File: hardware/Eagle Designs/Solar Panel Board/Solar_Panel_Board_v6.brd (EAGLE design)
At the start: 82.4 x 96.7 mm, 37 parts, among them J1 MOLEX_503763-0291MOLEX_503763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, J2 MOLEX_503763-0491MOLEX_503763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, J3 MOLEX_503763-0291MOLEX_503763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, U1 TMP36GSZ

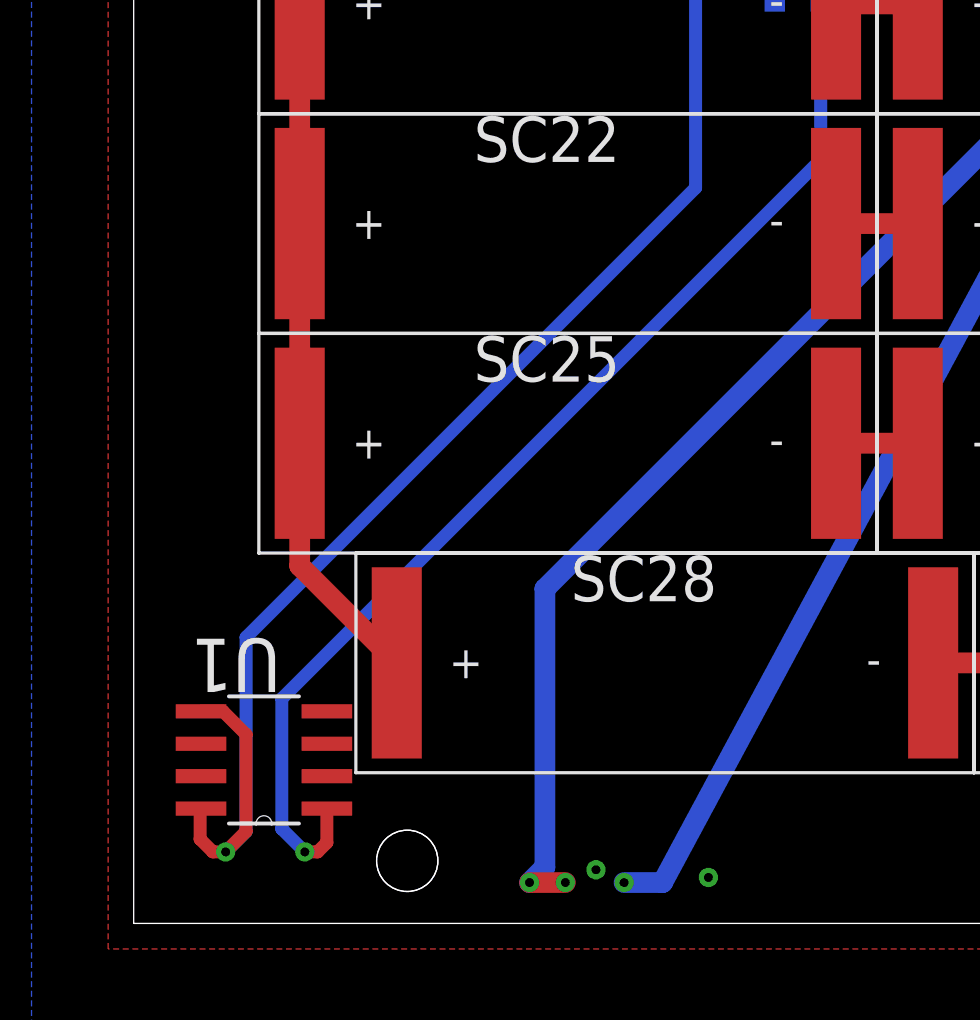
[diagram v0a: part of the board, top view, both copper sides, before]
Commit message: Updated OBC and Solar Panel boards
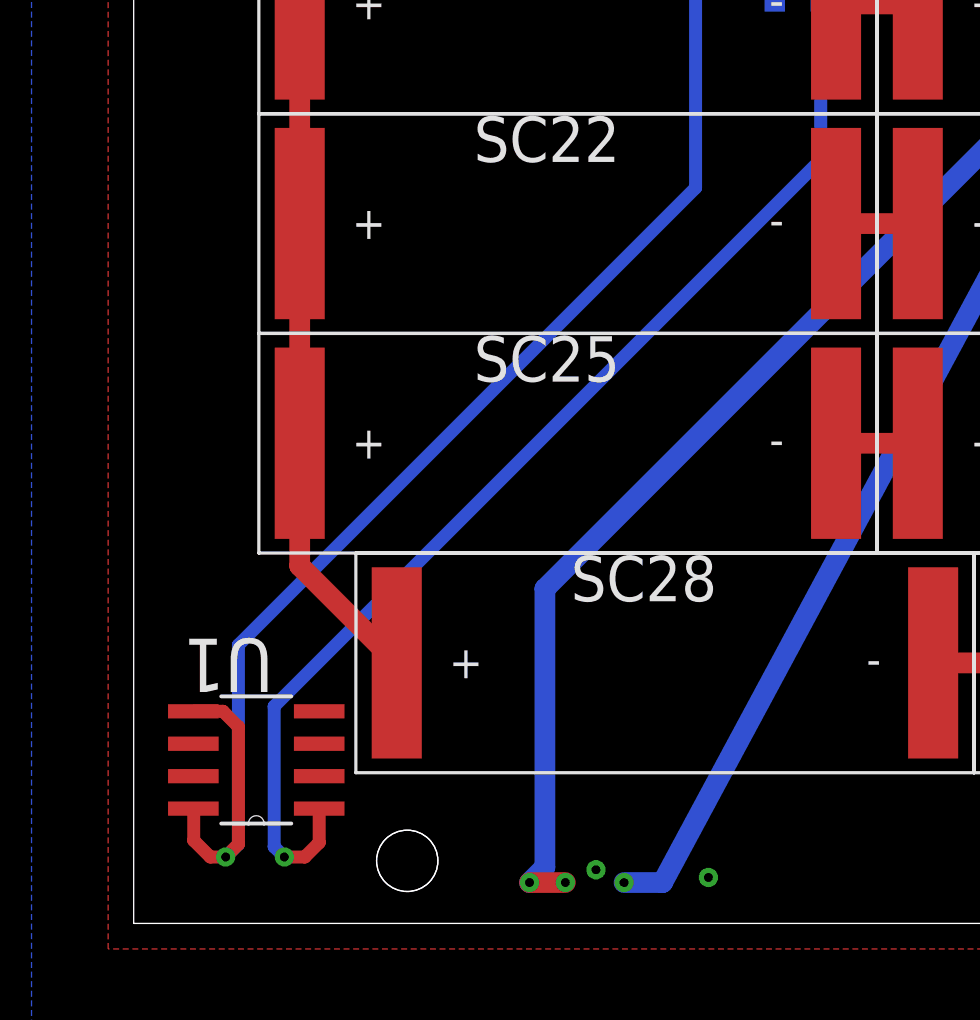
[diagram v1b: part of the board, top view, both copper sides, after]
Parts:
- moved U1 0.30 mm to (4.80, 6.40)
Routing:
- net VS+: track 84.2 -> 85.0 mm
- net N$12: track 45.0 -> 45.7 mm
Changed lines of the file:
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@@
 <attribute name="VOLTAGE_RATING" value="150V" x="43.6" y="70.8" size="1.778" layer="28" rot="MR0" display="off"/>
 </element>
-<element name="U1" library="TMP36GSZ" package="SOIC127P600X175-8N" value="TMP36GSZ" x="5.1" y="6.4" smashed="yes" rot="R180">
-<attribute name="NAME" x="5.760959375" y="11.146559375" size="2.08675" layer="25" ratio="10" rot="SR180"/>
-<attribute name="VALUE" x="8.55958125" y="12.12356875" size="2.08591875" layer="27" ratio="10" rot="SR180"/>
+<element name="U1" library="TMP36GSZ" package="SOIC127P600X175-8N" value="TMP36GSZ" x="4.8" y="6.4" smashed="yes" rot="R180">
+<attribute name="NAME" x="5.460959375" y="11.146559375" size="2.08675" layer="25" ratio="10" rot="SR180"/>
+<attribute name="VALUE" x="8.25958125" y="12.12356875" size="2.08591875" layer="27" ratio="10" rot="SR180"/>
 </element>
 <element name="J3" library="Molex - 503763-0291" package="MOLEX_503763-0291_0" value="MOLEX_503763-0291MOLEX_503763-0291_0_0" x="24.6" y="70.8" smashed="yes" rot="MR0">
@@
 <wire x1="22" y1="66.265" x2="22" y2="39.6" width="0.508" layer="16"/>
 <wire x1="22" y1="39.6" x2="22" y2="28.8" width="0.508" layer="16"/>
-<wire x1="22" y1="28.8" x2="4.4" y2="11.2" width="0.508" layer="16"/>
-<wire x1="4.4" y1="11.2" x2="4.4" y2="3.6" width="0.508" layer="16"/>
-<wire x1="2.6362" y1="8.305" x2="3.295" y2="8.305" width="0.508" layer="1"/>
-<wire x1="4.4" y1="3.6" x2="3.6" y2="2.8" width="0.508" layer="16"/>
-<via x="3.6" y="2.8" extent="1-16" drill="0.35"/>
-<wire x1="3.6" y1="2.8" x2="3.1" y2="2.8" width="0.508" layer="1"/>
-<wire x1="3.1" y1="2.8" x2="2.6" y2="3.3" width="0.508" layer="1"/>
-<wire x1="2.6" y1="3.3" x2="2.6" y2="4.4588" width="0.508" layer="1"/>
-<wire x1="2.6" y1="4.4588" x2="2.6362" y2="4.495" width="0.508" layer="1"/>
-<wire x1="2.6362" y1="8.305" x2="3.495" y2="8.305" width="0.508" layer="1"/>
-<wire x1="3.495" y1="8.305" x2="4.4" y2="7.4" width="0.508" layer="1"/>
-<wire x1="4.4" y1="7.4" x2="4.4" y2="3.6" width="0.508" layer="1"/>
-<wire x1="4.4" y1="3.6" x2="3.6" y2="2.8" width="0.508" layer="1"/>
+<wire x1="22" y1="28.8" x2="4.1" y2="10.9" width="0.508" layer="16"/>
+<wire x1="2.3362" y1="8.305" x2="2.995" y2="8.305" width="0.508" layer="1"/>
+<wire x1="2.35" y1="4.4812" x2="2.3362" y2="4.495" width="0.508" layer="1"/>
+<wire x1="2.3362" y1="8.305" x2="3.495" y2="8.305" width="0.508" layer="1"/>
+<wire x1="3.495" y1="8.305" x2="4.1" y2="7.7" width="0.508" layer="1"/>
+<wire x1="4.1" y1="3.1" x2="3.6" y2="2.6" width="0.508" layer="16"/>
+<via x="3.6" y="2.6" extent="1-16" drill="0.35"/>
+<wire x1="3.6" y1="2.6" x2="3" y2="2.6" width="0.508" layer="1"/>
+<wire x1="4.1" y1="10.9" x2="4.1" y2="3.1" width="0.508" layer="16"/>
+<wire x1="3" y1="2.6" x2="2.35" y2="3.25" width="0.508" layer="1"/>
+<wire x1="2.35" y1="3.25" x2="2.35" y2="4.4812" width="0.508" layer="1"/>
+<wire x1="4.1" y1="7.7" x2="4.1" y2="3.1" width="0.508" layer="1"/>
+<wire x1="4.1" y1="3.1" x2="3.6" y2="2.6" width="0.508" layer="1"/>
 </signal>
 <signal name="VOUT">
@@
 <contactref element="U1" pad="1"/>
 <contactref element="R1" pad="2"/>
-<via x="6.7" y="2.8" extent="1-16" drill="0.35"/>
-<wire x1="7.5638" y1="4.495" x2="7.5638" y2="3.1638" width="0.508" layer="1"/>
-<wire x1="7.5638" y1="3.1638" x2="7.2" y2="2.8" width="0.508" layer="1"/>
-<wire x1="7.2" y1="2.8" x2="6.7" y2="2.8" width="0.508" layer="1"/>
 <wire x1="26.9" y1="36.3" x2="26.9" y2="29.9" width="0.508" layer="16"/>
-<wire x1="6.7" y1="2.8" x2="5.8" y2="3.7" width="0.508" layer="16"/>
-<wire x1="26.9" y1="29.9" x2="5.8" y2="8.8" width="0.508" layer="16"/>
-<wire x1="5.8" y1="8.8" x2="5.8" y2="3.7" width="0.508" layer="16"/>
+<wire x1="26.9" y1="29.9" x2="5.5" y2="8.5" width="0.508" layer="16"/>
+<wire x1="5.5" y1="3" x2="5.9" y2="2.6" width="0.508" layer="16"/>
+<via x="5.9" y="2.6" extent="1-16" drill="0.35"/>
+<wire x1="5.9" y1="2.6" x2="6.7" y2="2.6" width="0.508" layer="1"/>
+<wire x1="6.7" y1="2.6" x2="7.2638" y2="3.1638" width="0.508" layer="1"/>
+<wire x1="7.2638" y1="3.1638" x2="7.2638" y2="4.495" width="0.508" layer="1"/>
+<wire x1="5.5" y1="8.5" x2="5.5" y2="3" width="0.508" layer="16"/>
 </signal>
 <signal name="N$16">
